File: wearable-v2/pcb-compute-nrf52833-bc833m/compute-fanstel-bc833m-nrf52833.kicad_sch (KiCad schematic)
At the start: 18 parts, among them J1 Conn_01x02_Pin, J5 HERALD_V2_CONN_PLUG, U6 BC833, U7 MX25R6435F, U8 PCF85063ATL, Y1 32.768kHz

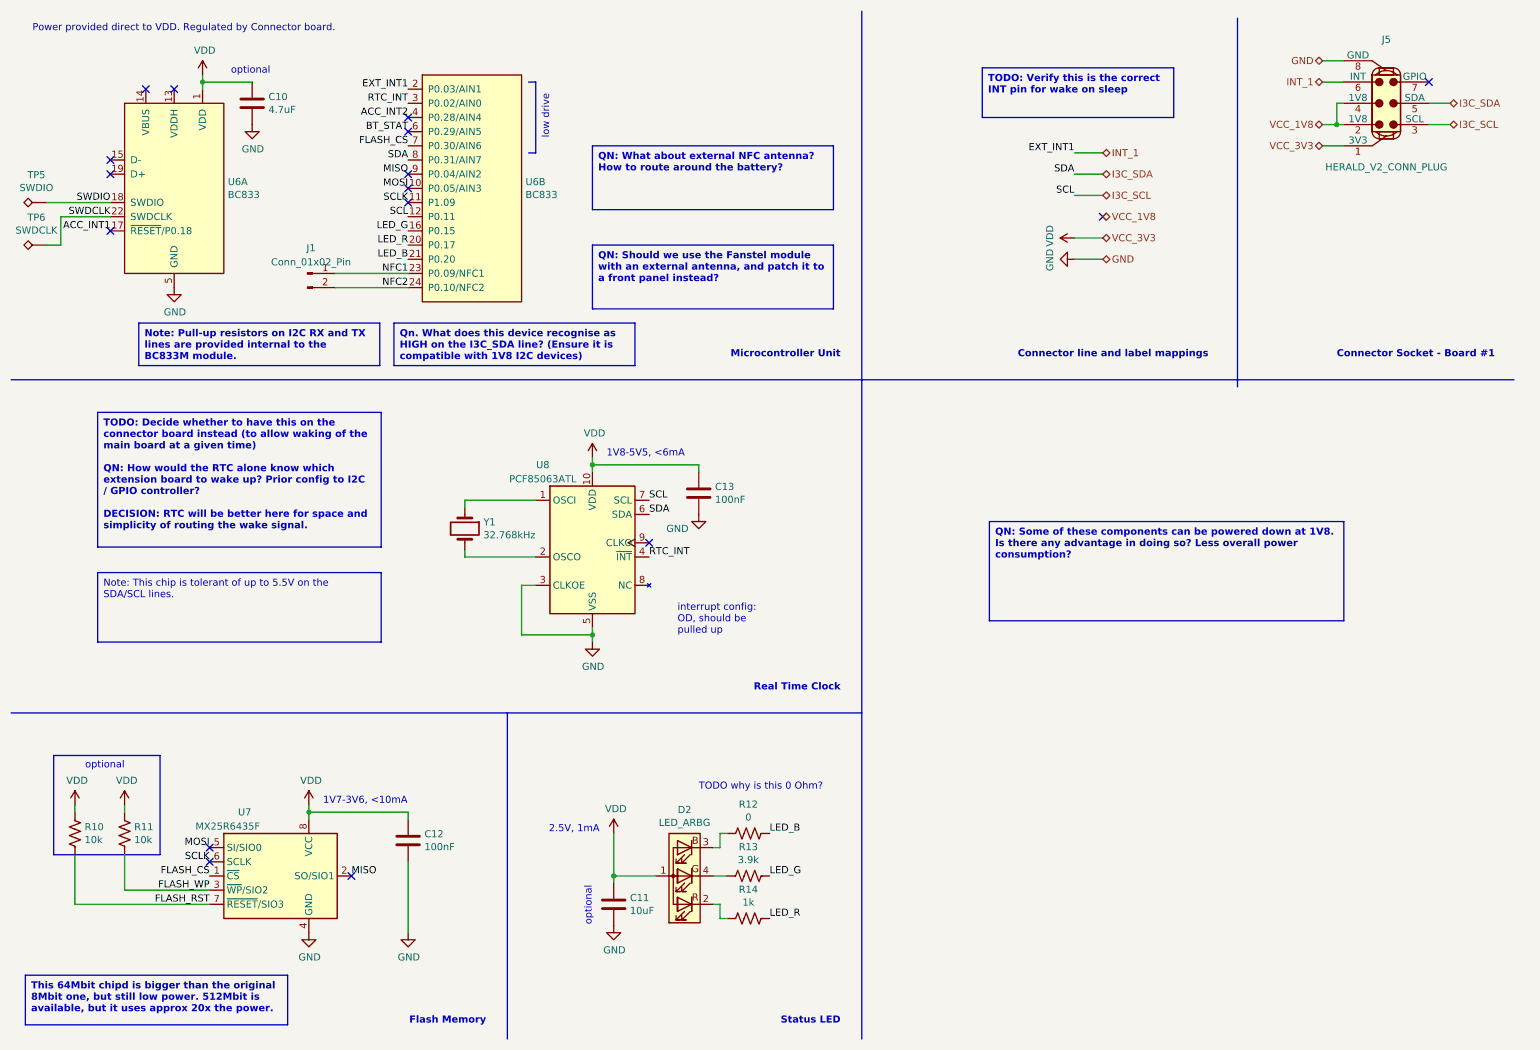
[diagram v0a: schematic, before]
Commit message: Refactoring PCB files
Moved major boards into their own files.
Corrected design elements for PCBWay manufacture.
Signed-off-by: Adam Fowler <adam@adamfowler.org>
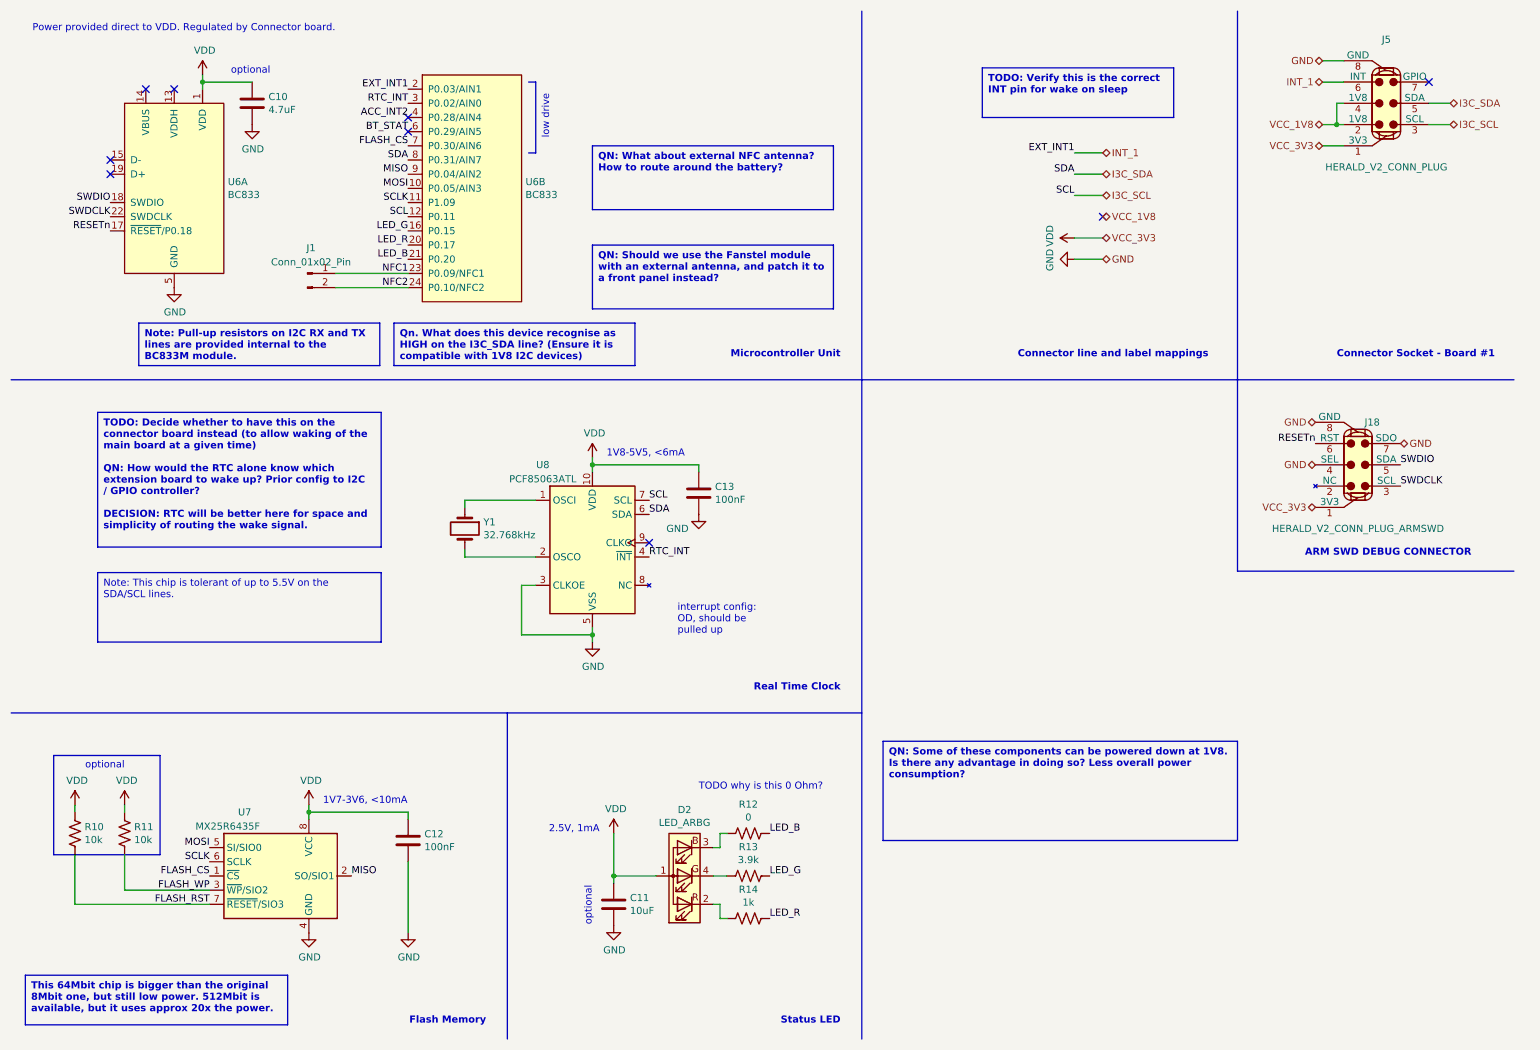
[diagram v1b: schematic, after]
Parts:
- removed TP5: SWDIO, TestPoint:TestPoint_Pad_D1.0mm, symbol Connector:TestPoint_Alt
- removed TP6: SWDCLK, TestPoint:TestPoint_Pad_D1.0mm, symbol Connector:TestPoint_Alt
- added J18: HERALD_V2_CONN_PLUG_ARMSWD, Herald_Extras:HERALD_V2_CONN_PORT, symbol Herald_Extras:HERALD_V2_CONN_PLUG_ARMSWD
- J5: footprint (none) -> Herald_Extras:HERALD_V2_CONN_PORT; MPN (none) -> 145861006024829+
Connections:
- net GND: now also J18.4 (SEL), J18.7 (SDO), J18.8 (GND)
- net SWDCLK: now also J18.3 (SCL)
- net SWDIO: now also J18.5 (SDA)
- net VDD: now also J18.1 (3V3)
- net ACC_INT1 renamed RESETn
- net RESETn: now also J18.6 (RST)
- no-connect marks 16 -> 9
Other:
- note added: "ARM SWD DEBUG CONNECTOR"

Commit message: Added accelerometer to compute module
Enable low power movement interrupt modes with just the compute module.
Signed-off-by: Adam Fowler <adam@adamfowler.org>
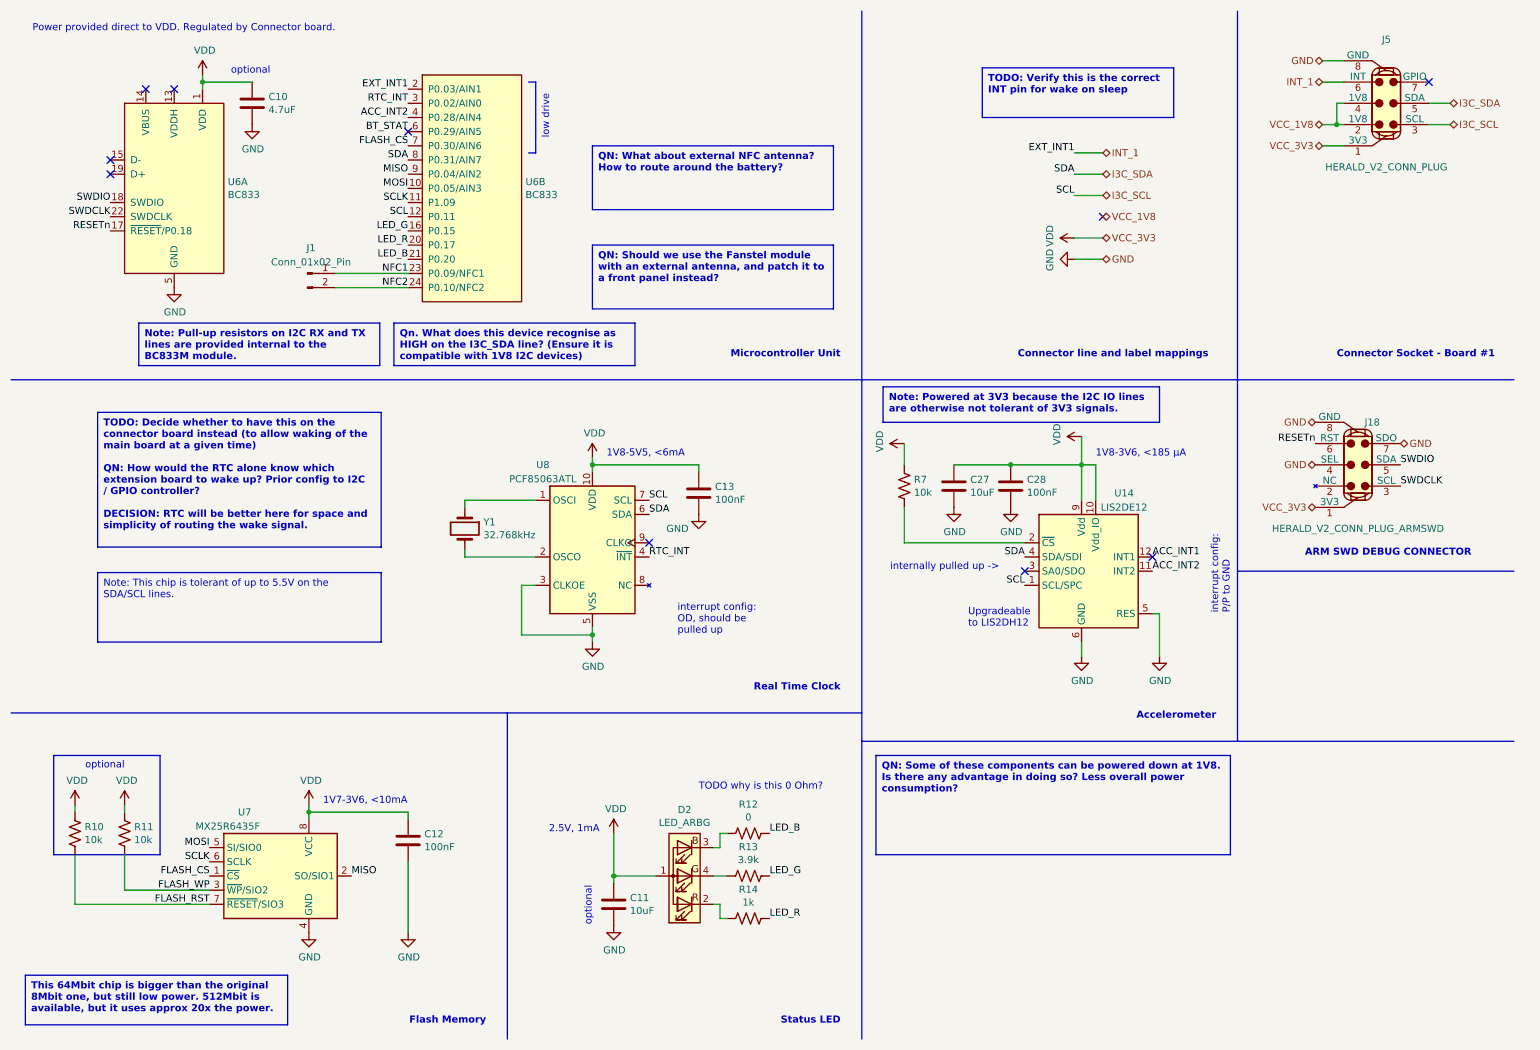
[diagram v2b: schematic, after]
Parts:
- added C27: 10uF, Capacitor_SMD:C_0402_1005Metric, symbol Device:C
- added C28: 100nF, Capacitor_SMD:C_0402_1005Metric, symbol Device:C
- added R7: 10k, Resistor_SMD:R_0402_1005Metric, symbol Device:R_US
- added U14: LIS2DE12, Package_LGA:LGA-12_2x2mm_P0.5mm, symbol Sensor_Motion:LIS2DE12
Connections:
- net ACC_INT2: now also U14.11 (INT2)
- net GND: now also C27.2, C28.2, U14.5 (RES), U14.6 (GND), U14.7 (GND), U14.8 (GND)
- net I3C_SCL: now also U14.1 (SCL/SPC)
- net I3C_SDA: now also U14.4 (SDA/SDI)
- net VDD: now also C27.1, C28.1, R7.1, U14.10 (Vdd_IO), U14.9 (Vdd)
- new net: R7.2, U14.2 (~{CS})
- new net ACC_INT1: U14.12 (INT1)
- no-connect marks 9 -> 10
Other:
- note added: "1V8-3V6, <185 µA"
- note added: "Accelerometer"
- note added: "Upgradeable to LIS2DH12"
- note added: "internally pulled up ->"
- note added: "interrupt config: P/P to GND"
